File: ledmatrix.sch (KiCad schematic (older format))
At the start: 56 parts, among them U58 sled1735

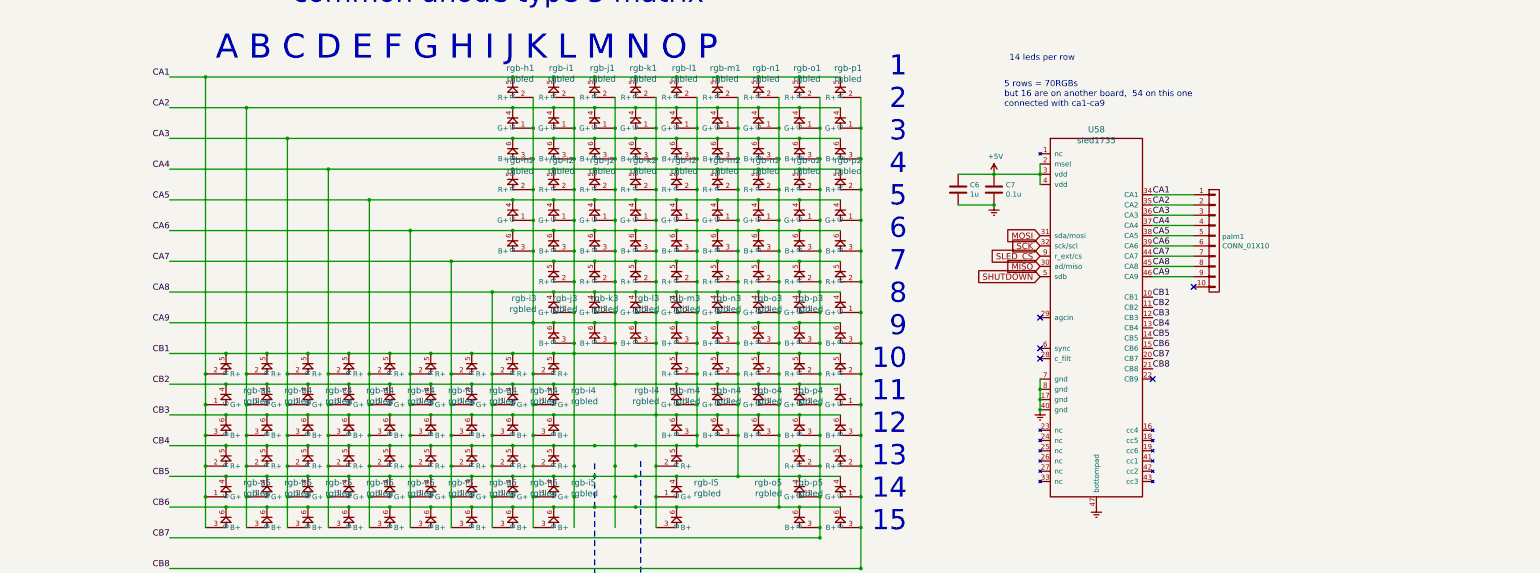
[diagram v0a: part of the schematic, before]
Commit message: full BOM info on parts
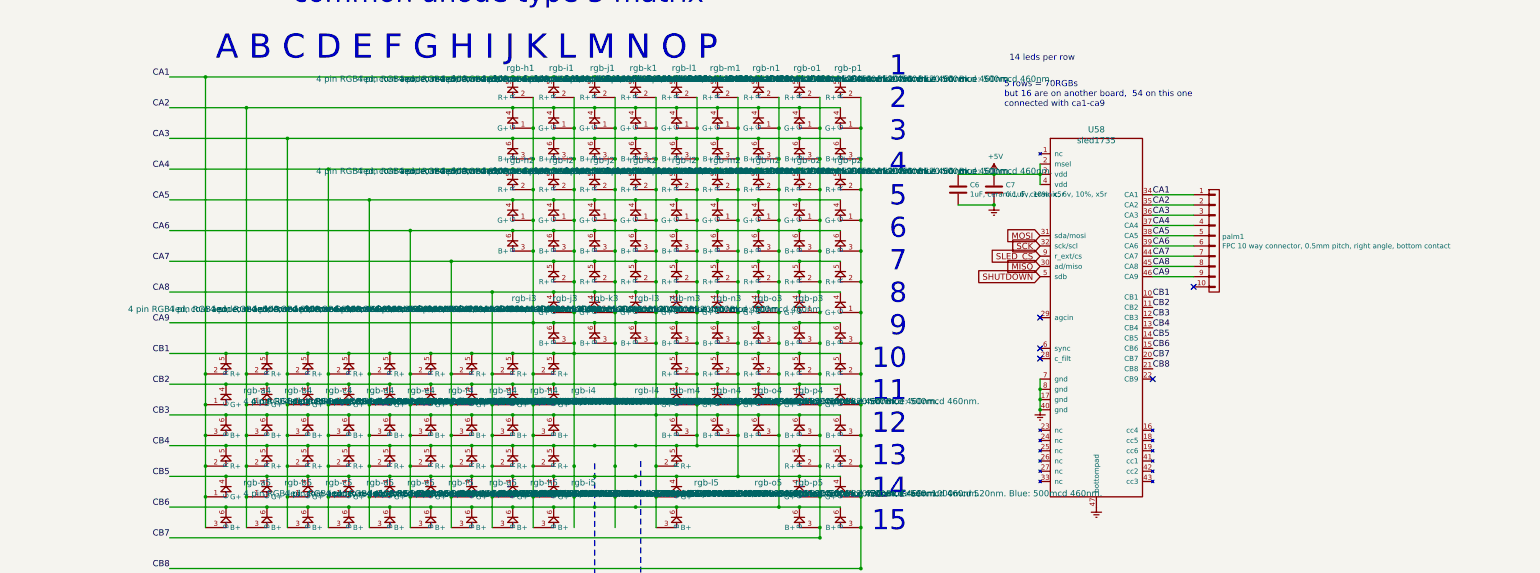
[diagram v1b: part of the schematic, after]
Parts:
- C6: value 1u -> 1uF, ceramic, 6v, 10%, x5r; supplier (none) -> any/open
- C7: value 0.1u -> 0.1uF, ceramic, 6v, 10%, x5r; supplier (none) -> any/open
- U58: footprint fp:QFN-56_EP_4.5x6.5_Pitch0.4mm -> fp:QFN-46_EP_4.5x6.5_Pitch0.4mm; supplier (none) -> sonix; supplier PN (none) -> SLED1735
- palm1: value CONN_01X10 -> FPC 10 way connector, 0.5mm pitch, right angle, bottom contact; supplier (none) -> any/open
- rgb-a4, rgb-a5, rgb-b4, rgb-b5, rgb-c4, rgb-c5, rgb-d4, rgb-d5, rgb-e4, rgb-e5, rgb-f4, rgb-f5, rgb-g4, rgb-g5, rgb-h2, rgb-h4, rgb-h5, rgb-i1, rgb-i2, rgb-i3, rgb-i4, rgb-i5, rgb-j1, rgb-j2, rgb-j3, rgb-k1, rgb-k2, rgb-k3, rgb-l1, rgb-l2, rgb-l3, rgb-l4, rgb-l5, rgb-m1, rgb-m2, rgb-m3, rgb-m4, rgb-n1, rgb-n2, rgb-n3, rgb-n4, rgb-o1, rgb-o2, rgb-o3, rgb-o4, rgb-o5, rgb-p1, rgb-p2, rgb-p3, rgb-p4, rgb-p5: value rgbled -> 4 pin RGB led, com anode, red: 500mcd 620nm. Green: 1000mcd 520nm. Blue: 500mcd 460nm.; supplier (none) -> any/open
- rgb-h1: value rgbled -> 4 pin RGB led, com anode, red: 500mcd 620nm. Green: 1000mcd 520nm. Blue: 500mcd 460nm.; farnell # 2765007 -> (none); supplier (none) -> any/open

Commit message: changed fp name of sled and added the J to part number
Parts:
- U58: footprint fp:QFN-46_EP_4.5x6.5_Pitch0.4mm -> fp:QFN-56_EP_4.5x6.5_Pitch0.4mm; MOQ (none) -> Value; leadtime (none) -> Value; supplier PN SLED1735 -> SLED1735J
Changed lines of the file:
@@
 F 0 "U58" H 10050 2987 60  0000 C CNN
 F 1 "sled1735" H 10050 2881 60  0000 C CNN
-F 2 "fp:QFN-46_EP_4.5x6.5_Pitch0.4mm" H 9850 2250 60  0001 C CNN
+F 2 "fp:QFN-56_EP_4.5x6.5_Pitch0.4mm" H 9850 2250 60  0001 C CNN
 F 3 "" H 9850 2250 60  0001 C CNN
 F 4 "sonix" H 0   0   60  0001 C CNN "supplier"
-F 5 "SLED1735" H 0   0   60  0001 C CNN "supplier PN"
+F 5 "SLED1735J" H 0   0   60  0001 C CNN "supplier PN"
+F 6 "Value" H 9850 2250 60  0001 C CNN "MOQ"
+F 7 "Value" H 9850 2250 60  0001 C CNN "leadtime"
 	1    9850 2250
 	1    0    0    -1

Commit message: layout wip
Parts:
- removed C7: 0.1uF, ceramic, 6v, 10%, x5r, Capacitors_SMD:C_0805, symbol C
- removed palm1: FPC 10 way connector, 0.5mm pitch, right angle, b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, fp:FPC_10_2046, symbol CONN_01X10
- added rgb-a2, rgb-a3, rgb-b2, rgb-b3, rgb-c1, rgb-c2, rgb-c3, rgb-d1, rgb-d3, rgb-e1, rgb-e3, rgb-f1, rgb-f2, rgb-f3, rgb-g1, rgb-g2: 4 pin RGB led, com anode, red: 500mcd 620nm. Gree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, fp:3528-4p, symbol rgbled
- C3: renamed from C6; footprint Capacitors_SMD:C_0805 -> Capacitors_SMD:C_0603; MOQ (none) -> Value; farnell # 1759422 -> 1865556; leadtime (none) -> Value; supplier PN (none) -> Value
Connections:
- net CA1: now also rgb-a2.1 (G+), rgb-a2.2 (R+), rgb-a2.3 (B+), rgb-a3.1 (G+), rgb-a3.2 (R+), rgb-a3.3 (B+), rgb-c1.5 (R-), rgb-d1.5 (R-), rgb-e1.5 (R-), rgb-f1.5 (R-), rgb-g1.5 (R-)
- net CA2: now also rgb-b2.1 (G+), rgb-b2.2 (R+), rgb-b2.3 (B+), rgb-b3.1 (G+), rgb-b3.2 (R+), rgb-b3.3 (B+), rgb-c1.4 (G-), rgb-d1.4 (G-), rgb-e1.4 (G-), rgb-f1.4 (G-), rgb-g1.4 (G-)
- net CA3: now also rgb-c1.6 (B-), rgb-c2.1 (G+), rgb-c2.2 (R+), rgb-c2.3 (B+), rgb-c3.1 (G+), rgb-c3.2 (R+), rgb-c3.3 (B+), rgb-d1.6 (B-), rgb-e1.6 (B-), rgb-f1.6 (B-), rgb-g1.6 (B-)
- net CA4: now also rgb-a2.5 (R-), rgb-b2.5 (R-), rgb-c1.1 (G+), rgb-c1.2 (R+), rgb-c1.3 (B+), rgb-c2.5 (R-), rgb-d3.1 (G+), rgb-d3.2 (R+), rgb-d3.3 (B+), rgb-f2.5 (R-), rgb-g2.5 (R-)
- net CA5: now also rgb-a2.4 (G-), rgb-b2.4 (G-), rgb-c2.4 (G-), rgb-d1.1 (G+), rgb-d1.2 (R+), rgb-d1.3 (B+), rgb-e3.1 (G+), rgb-e3.2 (R+), rgb-e3.3 (B+), rgb-f2.4 (G-), rgb-g2.4 (G-)
- net CA6: now also rgb-a2.6 (B-), rgb-b2.6 (B-), rgb-c2.6 (B-), rgb-e1.1 (G+), rgb-e1.2 (R+), rgb-e1.3 (B+), rgb-f2.6 (B-), rgb-f3.1 (G+), rgb-f3.2 (R+), rgb-f3.3 (B+), rgb-g2.6 (B-)
- net CA7: now also rgb-a3.5 (R-), rgb-b3.5 (R-), rgb-c3.5 (R-), rgb-d3.5 (R-), rgb-e3.5 (R-), rgb-f1.1 (G+), rgb-f1.2 (R+), rgb-f1.3 (B+), rgb-f2.1 (G+), rgb-f2.2 (R+), rgb-f2.3 (B+), rgb-f3.5 (R-)
- net ca8 renamed CA8
- net CA8: now also rgb-a3.4 (G-), rgb-b3.4 (G-), rgb-c3.4 (G-), rgb-d3.4 (G-), rgb-e3.4 (G-), rgb-f3.4 (G-), rgb-g1.1 (G+), rgb-g1.2 (R+), rgb-g1.3 (B+), rgb-g2.1 (G+), rgb-g2.2 (R+), rgb-g2.3 (B+)
- net ca9 renamed CA9
- net CA9: now also rgb-a3.6 (B-), rgb-b3.6 (B-), rgb-c3.6 (B-), rgb-d3.6 (B-), rgb-e3.6 (B-), rgb-f3.6 (B-)
- no-connect marks 5 -> 4
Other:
- note added: "2 lights for the LP: j5, k5"
- note added: "5 rows = 70RGBs max\n2 are on the low profile board"
- note removed: "2 lights for the LP"
- note removed: "5 rows = 70RGBs\nbut 16 are on another board, 54 on this one\nconnected with ca1-ca9"

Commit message: wip layout
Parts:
- added rgb-ISO-a2, rgb-ISO-j2: 4 pin RGB led, com anode, red: 500mcd 620nm. Gree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, fp:3528-4p, symbol rgbled
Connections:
- net CA1: now also rgb-ISO-a2.1 (G+), rgb-ISO-a2.2 (R+), rgb-ISO-a2.3 (B+)
- net CA4: now also rgb-ISO-a2.5 (R-), rgb-ISO-j2.5 (R-)
- net CA5: now also rgb-ISO-a2.4 (G-), rgb-ISO-j2.4 (G-)
- net CA6: now also rgb-ISO-a2.6 (B-), rgb-ISO-j2.6 (B-)
- net cb2: now also rgb-ISO-j2.1 (G+), rgb-ISO-j2.2 (R+), rgb-ISO-j2.3 (B+)
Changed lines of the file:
@@
 	1    0    0    -1
 $EndComp
+$Comp
+L rgbled rgb-ISO-a2
+U 1 1 5AE302CF
+P 1650 2450
+F 0 "rgb-ISO-a2" H 1481 2589 60  0000 R CNN
+F 1 "4 pin RGB led, com anode, red: 500mcd 620nm. Green: 1000mcd 520nm. Blue: 500mcd 460nm." H 1481 2483 60  0000 R CNN
+F 2 "fp:3528-4p" H 1650 2450 60  0001 C CNN
+F 3 "" H 1650 2450 60  0001 C CNN
+F 4 "any/open" H -4200 -1000 60  0001 C CNN "supplier"
+F 5 "Value" H 1650 2450 60  0001 C CNN "supplier PN"
+F 6 "Value" H 1650 2450 60  0001 C CNN "MOQ"
+F 7 "Value" H 1650 2450 60  0001 C CNN "leadtime"
+	1    1650 2450
+	-1   0    0    -1
+$EndComp
+Wire Wire Line
+	1650 1950 1650 1900
+Connection ~ 1650 1900
+Wire Wire Line
+	1450 2150 1350 2150
+Connection ~ 1350 2150
+Wire Wire Line
+	1650 2250 1650 2200
+Connection ~ 1650 2200
+Wire Wire Line
+	1450 2450 1350 2450
+Connection ~ 1350 2450
+Wire Wire Line
+	1650 2550 1650 2500
+Connection ~ 1650 2500
+Wire Wire Line
+	1450 2750 1350 2750
+Connection ~ 1350 2750
+$Comp
+L rgbled rgb-ISO-j2
+U 1 1 5AE31270
+P 5100 2450
+F 0 "rgb-ISO-j2" H 5175 3037 60  0000 C CNN
+F 1 "4 pin RGB led, com anode, red: 500mcd 620nm. Green: 1000mcd 520nm. Blue: 500mcd 460nm." H 5175 2931 60  0000 C CNN
+F 2 "fp:3528-4p" H 5100 2450 60  0001 C CNN
+F 3 "" H 5100 2450 60  0001 C CNN
+F 4 "any/open" H -50 50  60  0001 C CNN "supplier"
+F 5 "Value" H 5100 2450 60  0001 C CNN "supplier PN"
+F 6 "Value" H 5100 2450 60  0001 C CNN "MOQ"
+F 7 "Value" H 5100 2450 60  0001 C CNN "leadtime"
+	1    5100 2450
+	1    0    0    -1
+$EndComp
+Wire Wire Line
+	5300 2150 5350 2150
+Connection ~ 5350 2150
+Wire Wire Line
+	5300 2450 5350 2450
+Connection ~ 5350 2450
+Wire Wire Line
+	5300 2750 5350 2750
+Connection ~ 5350 2750
+Wire Wire Line
+	5100 2550 5100 2500
+Connection ~ 5100 2500
+Wire Wire Line
+	5100 2250 5100 2200
+Connection ~ 5100 2200
+Wire Wire Line
+	5100 1950 5100 1900
+Connection ~ 5100 1900
 $EndSCHEMATC

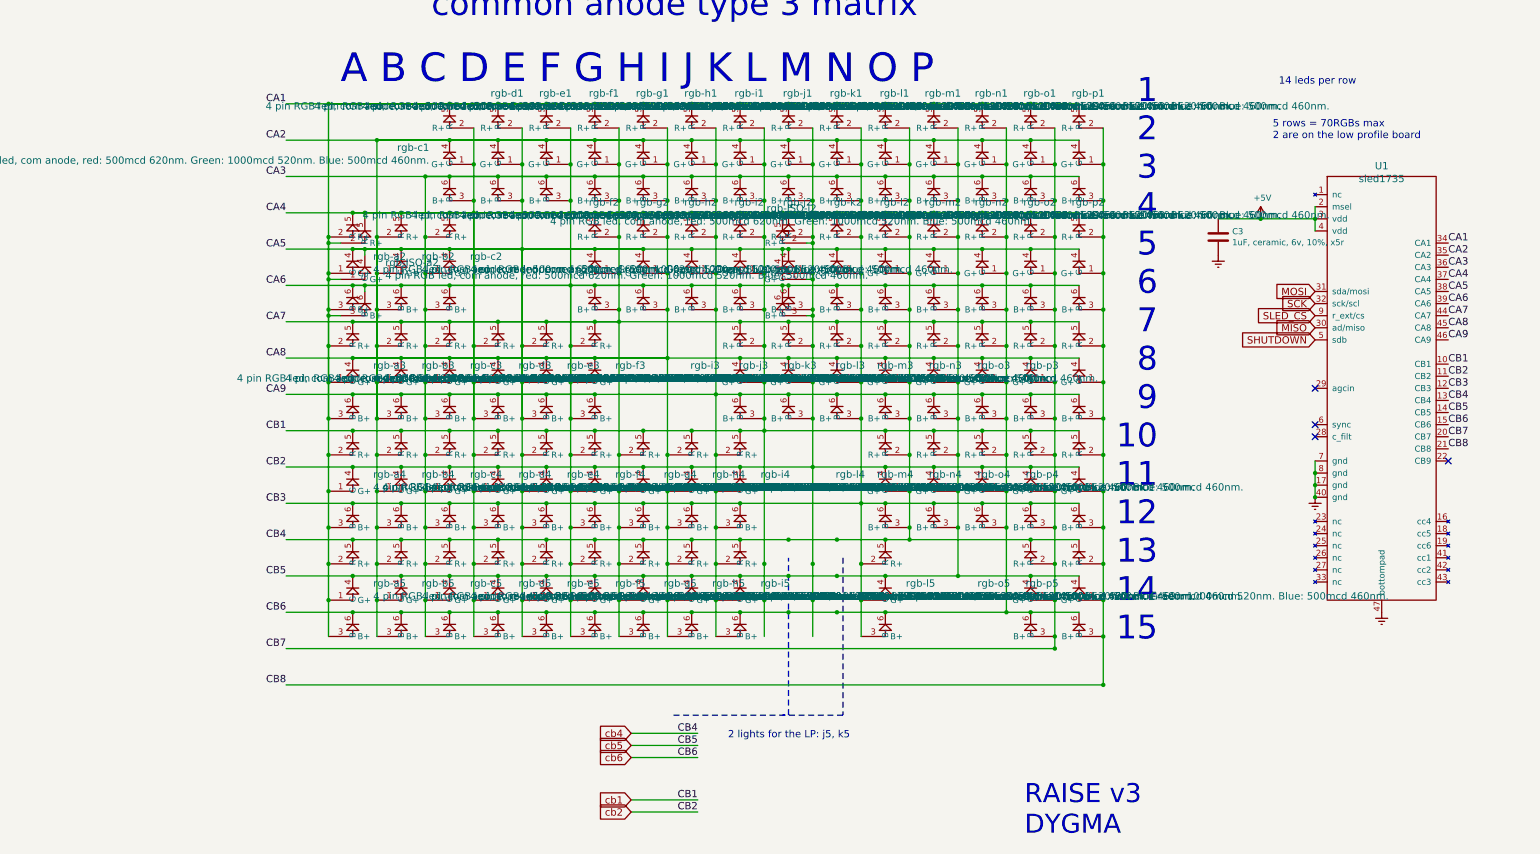
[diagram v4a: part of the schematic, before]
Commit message: changed switch and led numbering, re-laid out components, started routing
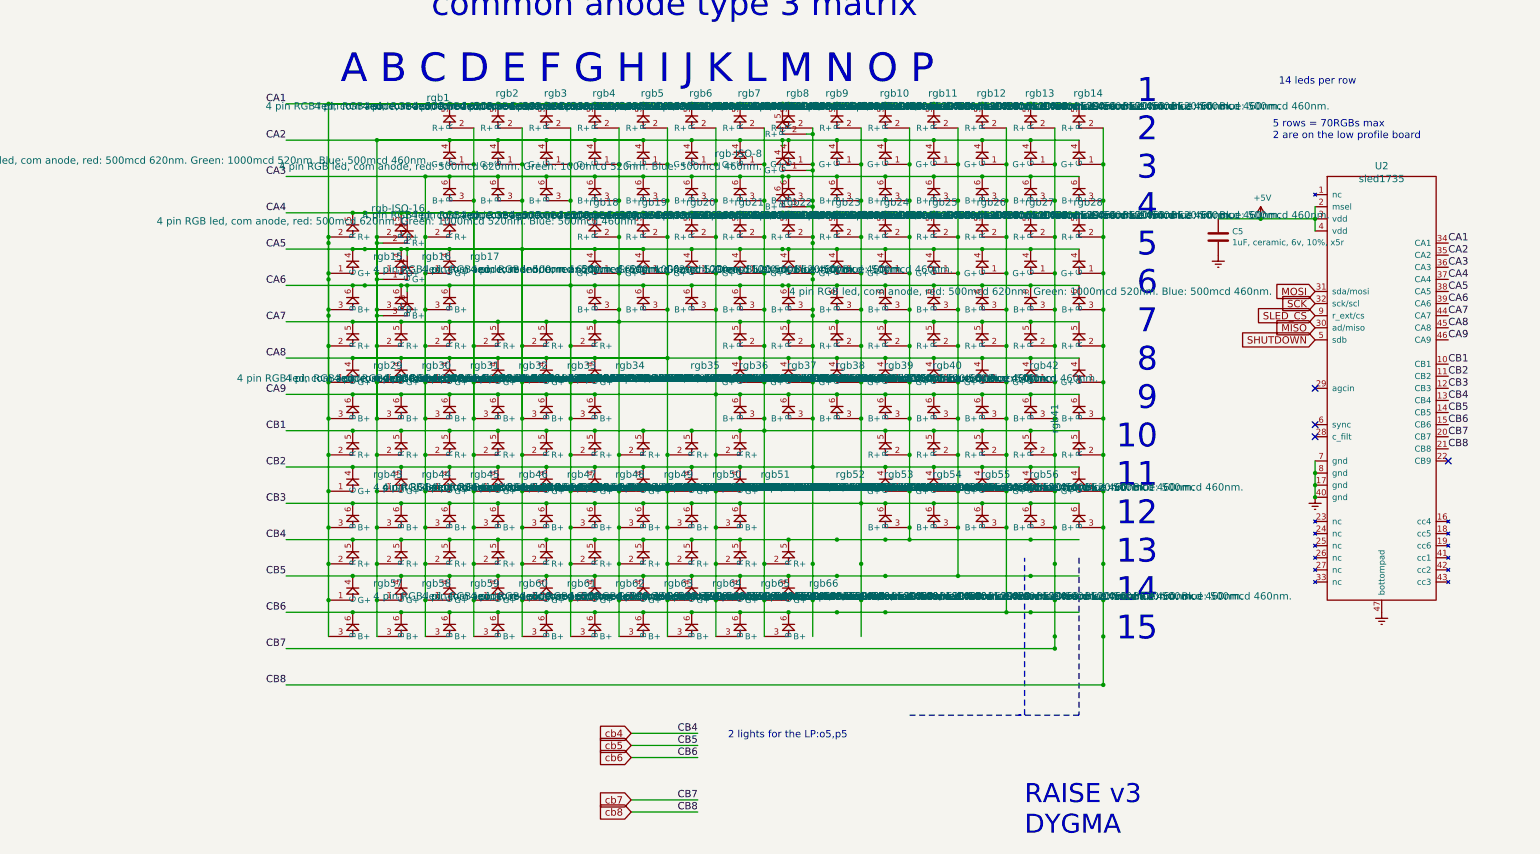
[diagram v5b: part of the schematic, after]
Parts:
- removed rgb-l5, rgb-o5, rgb-p5: 4 pin RGB led, com anode, red: 500mcd 620nm. Gree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, fp:3528-4p, symbol rgbled
- added rgb66: 4 pin RGB led, com anode, red: 500mcd 620nm. Gree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, fp:3528-4p, symbol rgbled
- rgb1: renamed from rgb-c1; MOQ (none) -> Value; leadtime (none) -> Value; supplier PN (none) -> Value
- rgb10: renamed from rgb-l1; MOQ (none) -> Value; leadtime (none) -> Value; supplier PN (none) -> Value
- rgb11: renamed from rgb-m1; MOQ (none) -> Value; leadtime (none) -> Value; supplier PN (none) -> Value
- rgb12: renamed from rgb-n1; MOQ (none) -> Value; leadtime (none) -> Value; supplier PN (none) -> Value
- rgb13: renamed from rgb-o1; MOQ (none) -> Value; leadtime (none) -> Value; supplier PN (none) -> Value
- rgb14: renamed from rgb-p1; MOQ (none) -> Value; leadtime (none) -> Value; supplier PN (none) -> Value
- rgb15: renamed from rgb-a2; MOQ (none) -> Value; leadtime (none) -> Value; supplier PN (none) -> Value
- rgb16: renamed from rgb-b2; MOQ (none) -> Value; leadtime (none) -> Value; supplier PN (none) -> Value
- rgb17: renamed from rgb-c2; MOQ (none) -> Value; leadtime (none) -> Value; supplier PN (none) -> Value
- rgb18: renamed from rgb-f2; MOQ (none) -> Value; leadtime (none) -> Value; supplier PN (none) -> Value
- rgb19: renamed from rgb-g2; MOQ (none) -> Value; leadtime (none) -> Value; supplier PN (none) -> Value
- rgb2: renamed from rgb-d1; MOQ (none) -> Value; leadtime (none) -> Value; supplier PN (none) -> Value
- rgb20: renamed from rgb-h2; MOQ (none) -> Value; leadtime (none) -> Value; supplier PN (none) -> Value
- rgb21: renamed from rgb-i2; MOQ (none) -> Value; leadtime (none) -> Value; supplier PN (none) -> Value
- rgb22: renamed from rgb-j2; MOQ (none) -> Value; leadtime (none) -> Value; supplier PN (none) -> Value
- rgb23: renamed from rgb-k2; MOQ (none) -> Value; leadtime (none) -> Value; supplier PN (none) -> Value
- rgb24: renamed from rgb-l2; MOQ (none) -> Value; leadtime (none) -> Value; supplier PN (none) -> Value
- rgb25: renamed from rgb-m2; MOQ (none) -> Value; leadtime (none) -> Value; supplier PN (none) -> Value
- rgb26: renamed from rgb-n2; MOQ (none) -> Value; leadtime (none) -> Value; supplier PN (none) -> Value
- rgb27: renamed from rgb-o2; MOQ (none) -> Value; leadtime (none) -> Value; supplier PN (none) -> Value
- rgb28: renamed from rgb-p2; MOQ (none) -> Value; leadtime (none) -> Value; supplier PN (none) -> Value
- rgb29: renamed from rgb-a3; MOQ (none) -> Value; leadtime (none) -> Value; supplier PN (none) -> Value
- rgb3: renamed from rgb-e1; MOQ (none) -> Value; leadtime (none) -> Value; supplier PN (none) -> Value
- rgb30: renamed from rgb-b3; MOQ (none) -> Value; leadtime (none) -> Value; supplier PN (none) -> Value
- rgb31: renamed from rgb-c3; MOQ (none) -> Value; leadtime (none) -> Value; supplier PN (none) -> Value
- rgb32: renamed from rgb-d3; MOQ (none) -> Value; leadtime (none) -> Value; supplier PN (none) -> Value
- rgb33: renamed from rgb-e3; MOQ (none) -> Value; leadtime (none) -> Value; supplier PN (none) -> Value
- rgb34: renamed from rgb-f3; MOQ (none) -> Value; leadtime (none) -> Value; supplier PN (none) -> Value
- rgb35: renamed from rgb-i3; MOQ (none) -> Value; leadtime (none) -> Value; supplier PN (none) -> Value
- rgb36: renamed from rgb-j3; MOQ (none) -> Value; leadtime (none) -> Value; supplier PN (none) -> Value
- rgb37: renamed from rgb-k3; MOQ (none) -> Value; leadtime (none) -> Value; supplier PN (none) -> Value
- rgb38: renamed from rgb-l3; MOQ (none) -> Value; leadtime (none) -> Value; supplier PN (none) -> Value
- rgb39: renamed from rgb-m3; MOQ (none) -> Value; leadtime (none) -> Value; supplier PN (none) -> Value
- rgb4: renamed from rgb-f1; MOQ (none) -> Value; leadtime (none) -> Value; supplier PN (none) -> Value
- rgb40: renamed from rgb-n3; MOQ (none) -> Value; leadtime (none) -> Value; supplier PN (none) -> Value
- rgb41: renamed from rgb-o3; MOQ (none) -> Value; leadtime (none) -> Value; supplier PN (none) -> Value
- rgb42: renamed from rgb-p3; MOQ (none) -> Value; leadtime (none) -> Value; supplier PN (none) -> Value
- rgb43: renamed from rgb-a4; MOQ (none) -> Value; leadtime (none) -> Value; supplier PN (none) -> Value
- rgb44: renamed from rgb-b4; MOQ (none) -> Value; leadtime (none) -> Value; supplier PN (none) -> Value
- rgb45: renamed from rgb-c4; MOQ (none) -> Value; leadtime (none) -> Value; supplier PN (none) -> Value
- rgb46: renamed from rgb-d4; MOQ (none) -> Value; leadtime (none) -> Value; supplier PN (none) -> Value
- rgb47: renamed from rgb-e4; MOQ (none) -> Value; leadtime (none) -> Value; supplier PN (none) -> Value
- rgb48: renamed from rgb-f4; MOQ (none) -> Value; leadtime (none) -> Value; supplier PN (none) -> Value
- rgb49: renamed from rgb-g4; MOQ (none) -> Value; leadtime (none) -> Value; supplier PN (none) -> Value
- rgb50: renamed from rgb-h4; MOQ (none) -> Value; leadtime (none) -> Value; supplier PN (none) -> Value
- rgb51: renamed from rgb-i4; MOQ (none) -> Value; leadtime (none) -> Value; supplier PN (none) -> Value
- rgb52: renamed from rgb-l4; MOQ (none) -> Value; leadtime (none) -> Value; supplier PN (none) -> Value
- rgb53: renamed from rgb-m4; MOQ (none) -> Value; leadtime (none) -> Value; supplier PN (none) -> Value
- rgb54: renamed from rgb-n4; MOQ (none) -> Value; leadtime (none) -> Value; supplier PN (none) -> Value
- rgb55: renamed from rgb-o4; MOQ (none) -> Value; leadtime (none) -> Value; supplier PN (none) -> Value
- rgb56: renamed from rgb-p4; MOQ (none) -> Value; leadtime (none) -> Value; supplier PN (none) -> Value
- rgb57: renamed from rgb-a5; MOQ (none) -> Value; leadtime (none) -> Value; supplier PN (none) -> Value
- rgb58: renamed from rgb-b5; MOQ (none) -> Value; leadtime (none) -> Value; supplier PN (none) -> Value
- rgb59: renamed from rgb-c5; MOQ (none) -> Value; leadtime (none) -> Value; supplier PN (none) -> Value
- rgb6: renamed from rgb-h1; MOQ (none) -> Value; leadtime (none) -> Value; supplier PN (none) -> Value
- rgb60: renamed from rgb-d5; MOQ (none) -> Value; leadtime (none) -> Value; supplier PN (none) -> Value
- rgb61: renamed from rgb-e5; MOQ (none) -> Value; leadtime (none) -> Value; supplier PN (none) -> Value
- rgb62: renamed from rgb-f5; MOQ (none) -> Value; leadtime (none) -> Value; supplier PN (none) -> Value
- rgb63: renamed from rgb-g5; MOQ (none) -> Value; leadtime (none) -> Value; supplier PN (none) -> Value
- rgb64: renamed from rgb-h5; MOQ (none) -> Value; leadtime (none) -> Value; supplier PN (none) -> Value
- rgb65: renamed from rgb-i5; MOQ (none) -> Value; leadtime (none) -> Value; supplier PN (none) -> Value
- rgb7: renamed from rgb-i1; MOQ (none) -> Value; leadtime (none) -> Value; supplier PN (none) -> Value
- rgb8: renamed from rgb-j1; MOQ (none) -> Value; leadtime (none) -> Value; supplier PN (none) -> Value
- rgb9: renamed from rgb-k1; MOQ (none) -> Value; leadtime (none) -> Value; supplier PN (none) -> Value
- renumbered C3 to C5, U58 to U2, rgb-ISO-j2 to rgb-ISO-16, rgb-ISO-a2 to rgb-ISO-8, rgb-g1 to rgb5
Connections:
- net labels added: cb7, cb8
- net labels removed: cb1, cb2
- wire segments 69 -> 70
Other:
- note added: "2 lights for the LP:o5,p5\n"
- note removed: "2 lights for the LP: j5, k5"
- moved on the sheet: rgb-ISO-16, rgb-ISO-8

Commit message: moved footprints to submodule
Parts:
- C5: footprint Capacitors_SMD:C_0603 -> raise_fp:C_0603
- U2: footprint fp:QFN-56_EP_4.5x6.5_Pitch0.4mm -> raise_fp:QFN-56_EP_4.5x6.5_Pitch0.4mm
- rgb-ISO-16, rgb-ISO-8, rgb1, rgb10, rgb11, rgb12, rgb13, rgb14, rgb15, rgb16, rgb17, rgb18, rgb19, rgb2, rgb20, rgb21, rgb22, rgb23, rgb24, rgb25, rgb26, rgb27, rgb28, rgb29, rgb3, rgb30, rgb31, rgb32, rgb33, rgb34, rgb35, rgb36, rgb37, rgb38, rgb39, rgb4, rgb40, rgb41, rgb42, rgb43, rgb44, rgb45, rgb46, rgb47, rgb48, rgb49, rgb5, rgb50, rgb51, rgb52, rgb53, rgb54, rgb55, rgb56, rgb57, rgb58, rgb59, rgb6, rgb60, rgb61, rgb62, rgb63, rgb64, rgb65, rgb66, rgb7, rgb8, rgb9: footprint fp:3528-4p -> raise_fp:3528-4p

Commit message: reverse leds
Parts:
- rgb-ISO-16, rgb-ISO-8, rgb1, rgb10, rgb11, rgb12, rgb13, rgb14, rgb15, rgb16, rgb17, rgb18, rgb19, rgb2, rgb20, rgb21, rgb22, rgb23, rgb24, rgb25, rgb26, rgb27, rgb28, rgb29, rgb3, rgb30, rgb31, rgb32, rgb33, rgb34, rgb4, rgb5, rgb6, rgb7, rgb8, rgb9: footprint raise_fp:3528-4p -> raise_fp:3528-4p-rev
